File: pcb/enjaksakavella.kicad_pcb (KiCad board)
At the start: 2 copper layers, 101.6 x 53.3 mm, 33 parts, among them J1 DB9_Female, J10 Conn_01x06, J11 Conn_01x06, J12 Conn_02x03_Odd_Even, J13 Conn_01x06, J2 Conn_02x05_Odd_Even, J3 Conn_02x03_Odd_Even, J4 Conn_02x05_Odd_Even, J5 Conn_01x06, J6 Conn_01x03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

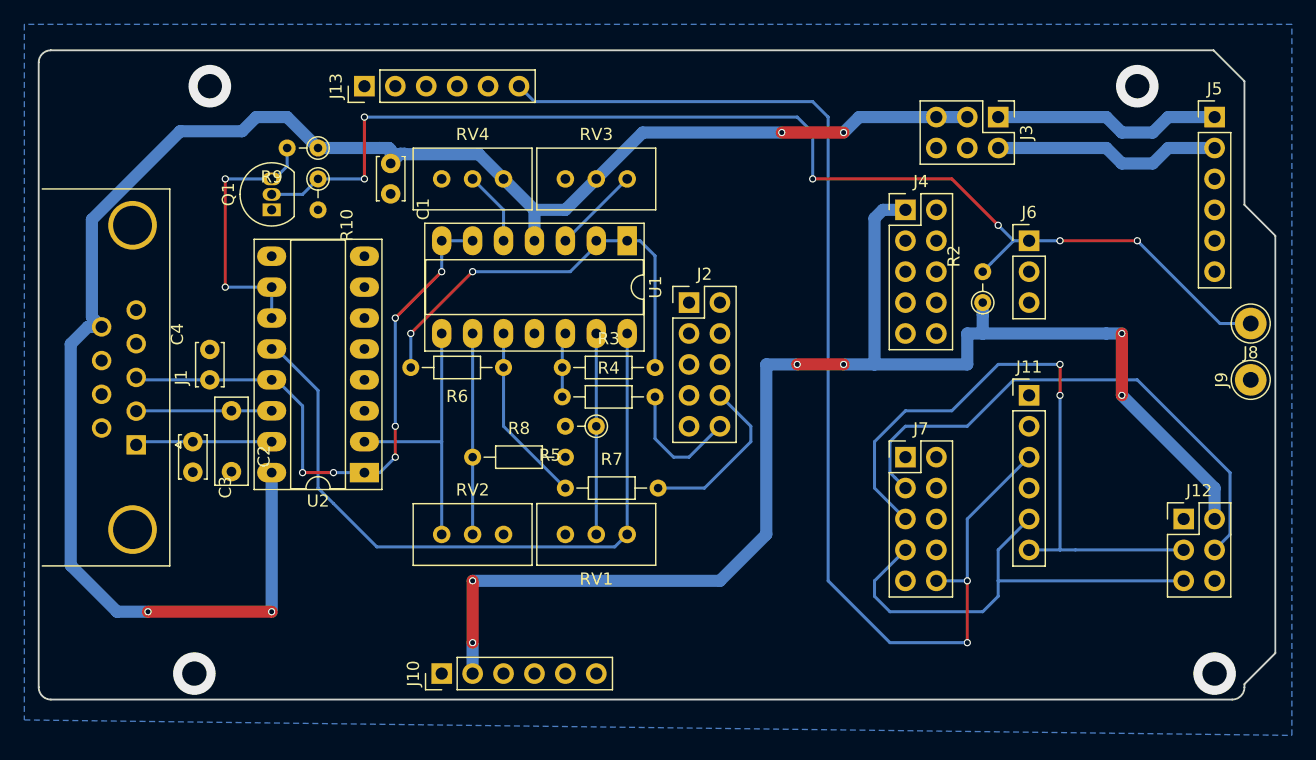
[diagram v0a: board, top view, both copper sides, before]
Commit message: Update pcb files to new KiCad version
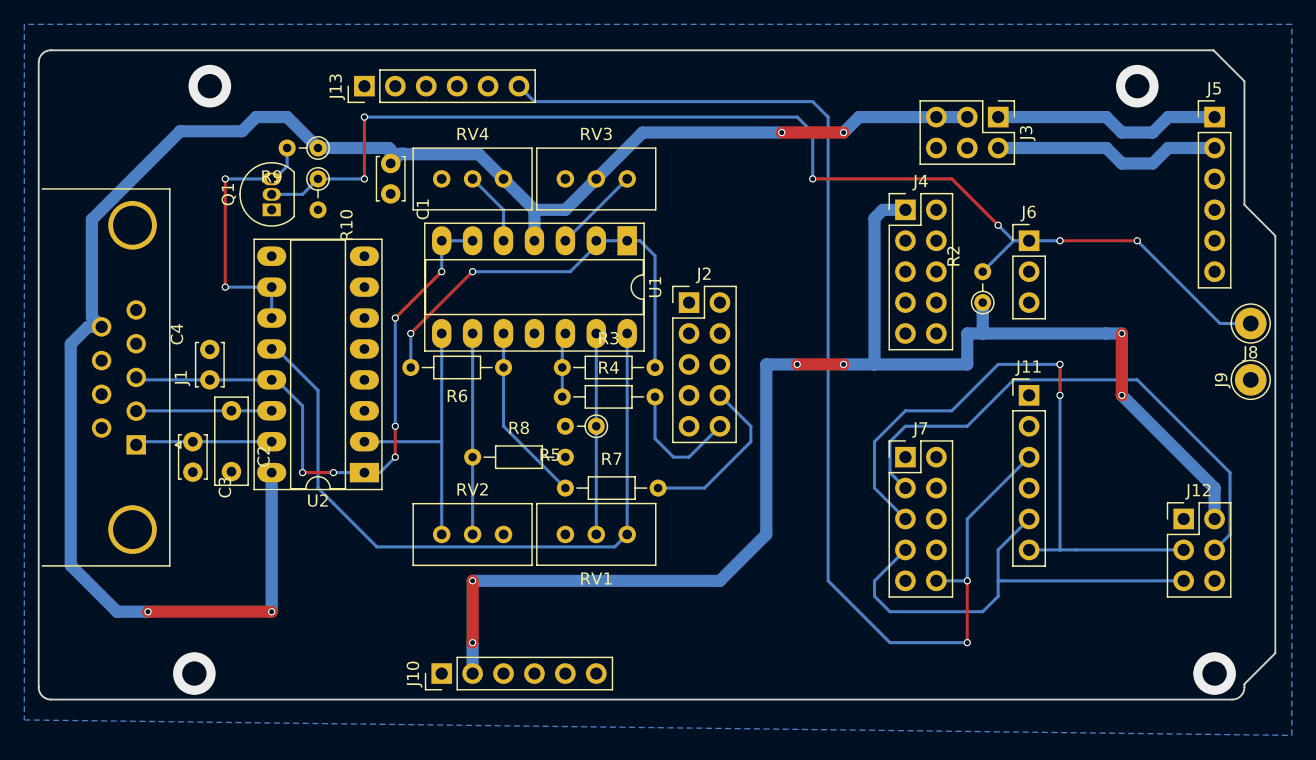
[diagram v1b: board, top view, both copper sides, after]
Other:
- net class Default removed
